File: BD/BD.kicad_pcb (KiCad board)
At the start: 2 copper layers, 95 x 90 mm, 57 parts, among them P1 bateria 7.4 V, P2 HC-06 (BT), P3 SILNIK1, P4 Modol startujacy, P5 PROGRAMAT, P7 SILNIK2, SW1 SPST, SW2 SW_PUSH, U1 LM1117, U10 TB6612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

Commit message: mozna drukowac?
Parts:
- moved R10 1.42 mm to (107.1, 66.6)
- moved R9 1.42 mm to (104.1, 66.6)
- moved U8 1.42 mm to (105.8, 63.7)
- turned C15 to 270 degrees
- turned C16 to 90 degrees
- turned C19 to 90 degrees
- turned C20 to 90 degrees
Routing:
- net SHARP4: track 43.7 -> 2.30 mm
- net GND: track 145.5 -> 182.6 mm, vias 2 -> 7
- net KTIR1: track 74.6 -> 95.8 mm
- net +5V: track 188.7 -> 174.5 mm
- net (no net): track 13.9 -> 0.00 mm, vias 5 -> 0
- net +3V3: track 458.2 -> 465.5 mm
- net BT2: track 33.5 -> 38.9 mm
- net PROG1: track 49.7 -> 55.0 mm
- net Net-(P3-Pad2): track 12.6 -> 7.67 mm, vias 1 -> 0
- net Net-(P3-Pad1): track 22.3 -> 17.9 mm, vias 1 -> 0
- net Net-(P7-Pad2): track 11.2 -> 6.88 mm, vias 1 -> 0
- net RESET: track 22.5 -> 26.3 mm
- net PROG2: track 39.5 -> 43.0 mm
- net VCC: track 132.8 -> 135.2 mm
- net KTIR2: track 72.5 -> 70.5 mm
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
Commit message: 2 wersja plytek
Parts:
- C1, C13, C2, C3, C4: footprint Capacitors_SMD:C_0402 -> Capacitors_SMD:C_0805_HandSoldering
- C10, C11, C12: footprint Capacitors_SMD:C_0603 -> Capacitors_SMD:C_0603_HandSoldering
- C14, C16, C18, C19, C22, C9: footprint Capacitors_SMD:C_0805 -> Capacitors_SMD:C_0805_HandSoldering
- C15, C17, C20, C21, C5, C6, C7, C8: footprint Capacitors_Tantalum_SMD:TantalC_SizeR_EIA-2012 -> Capacitors_Tantalum_SMD:Tantalum_Case-A_EIA-3216-18_Hand
- R1, R11, R12, R2, R3, R4, R5, R6: footprint Resistors_SMD:R_0805 -> Resistors_SMD:R_0805_HandSoldering
- R10, R7, R8, R9: footprint Resistors_SMD:R_0603 -> Resistors_SMD:R_0603_HandSoldering
- SP1: footprint Buzzer_moj -> Buzzers_Beepers:Buzzer_12x9.5RM7.6
- moved C17 3.79 mm to (171.1, 130.6), turned to 270 degrees
- moved C15 3.54 mm to (124.4, 130.2), turned to 90 degrees
- moved C16 2.87 mm to (126.8, 132.2)
- moved C14 2.21 mm to (144.6, 121.6)
- moved C13 2.01 mm to (144.6, 119.3)
- moved C19 1.35 mm to (127.2, 137.7)
- moved C18 1.26 mm to (168.1, 134.3)
- moved C22 0.75 mm to (167.8, 139.8)
- moved R2 0.73 mm to (115.2, 100.7)
- moved R9 0.72 mm to (103.4, 66.6)
- moved R10 0.65 mm to (107.8, 66.6)
- moved C10 0.59 mm to (155.2, 107.1)
- moved C4 0.59 mm to (168.7, 90.1)
- moved C21 0.44 mm to (171.0, 138.9), turned to 90 degrees
- moved C2 0.39 mm to (115.2, 105.9)
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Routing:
- net SHARP4: track 2.30 -> 55.7 mm
- net +3V3: track 465.5 -> 501.6 mm, vias 5 -> 6
- net +5V: track 174.5 -> 192.3 mm
- net GND: track 182.6 -> 196.2 mm
- net SHARP1: track 40.6 -> 51.2 mm
- net VCC: track 135.2 -> 141.5 mm, vias 2 -> 3
- net Net-(D1-Pad2): track 5.71 -> 10.8 mm
- net RESET: track 26.3 -> 30.9 mm, vias 0 -> 1
- net KTIR1: track 95.8 -> 97.8 mm
- net PROG1: track 55.0 -> 54.1 mm
- net Net-(R2-Pad1): track 7.24 -> 6.48 mm
- net SHARP3: track 49.8 -> 50.5 mm
- net Net-(R12-Pad1): track 20.3 -> 20.9 mm

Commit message: tak
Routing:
- net +3V3: track 501.6 -> 488.2 mm, vias 6 -> 4
- net GND: track 196.2 -> 193.2 mm, vias 7 -> 6
- net VCC: track 141.5 -> 139.1 mm, vias 3 -> 2
- net RESET: track 30.9 -> 32.1 mm
- net KTIR1: track 97.8 -> 98.4 mm
- net +5V: track 192.3 -> 192.7 mm, vias 7 -> 4

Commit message: taak
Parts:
- moved P1 1.25 mm to (137.4, 91.8)
- moved SW1 0.50 mm to (137.4, 99.4), turned to 180 degrees
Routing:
- net +5V: track 192.7 -> 185.5 mm
- net VCC: track 139.1 -> 144.8 mm
- net GND: track 193.2 -> 190.3 mm
- net Net-(P1-Pad2): track 6.35 -> 5.11 mm
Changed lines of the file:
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@@
     (thickness 1.6)
     (drawings 14)
-    (tracks 775)
+    (tracks 776)
     (zones 0)
     (modules 57)
@@
   )
   (module Socket_Strips:Socket_Strip_Straight_1x02 (layer F.Cu)
-    (at 137.85 90.61 270)
+    (at 137.41 91.78 270)
     (descr "Through hole socket strip")
     (tags "socket strip")
@@
   )
   (module Buttons_Switches_ThroughHole:SW_DIP_x1_Slide (layer F.Cu)
-    (at 137.86 99.48 270)
+    (at 137.36 99.41 180)
     (descr "CTS Electrocomponents, Series 206/208")
-    (fp_text reference SW1 (at 0 -10 270) (layer F.SilkS)
-      (effects (font (size 1 1) (thickness 0.15)))
-    )
-    (fp_text value SPST (at 0.5 2.4 270) (layer F.Fab)
+    (fp_text reference SW1 (at 0 -10 180) (layer F.SilkS)
+      (effects (font (size 1 1) (thickness 0.15)))
+    )
+    (fp_text value SPST (at 0.5 2.4 180) (layer F.Fab)
       (effects (font (size 1 1) (thickness 0.15)))
     )
@@
     (fp_line (start 0.64 -1.78) (end 0.64 -5.84) (layer F.SilkS) (width 0.15))
     (fp_line (start 0.64 -5.84) (end -0.64 -5.84) (layer F.SilkS) (width 0.15))
-    (pad 1 thru_hole rect (at 0 0 270) (size 1.524 1.824) (drill 0.762) (layers *.Cu *.Mask)
+    (pad 1 thru_hole rect (at 0 0 180) (size 1.524 1.824) (drill 0.762) (layers *.Cu *.Mask)
       (net 13 "Net-(P1-Pad2)"))
-    (pad 2 thru_hole oval (at 0 -7.62 270) (size 1.524 1.824) (drill 0.762) (layers *.Cu *.Mask)
+    (pad 2 thru_hole oval (at 0 -7.62 180) (size 1.524 1.824) (drill 0.762) (layers *.Cu *.Mask)
       (net 6 VCC))
     (model Buttons_Switches_ThroughHole.3dshapes/SW_DIP_x1_Slide.wrl
@@
   (gr_line (start 165 150) (end 115 150) (layer Edge.Cuts) (width 0.15))
   (gr_line (start 100 60) (end 195 60) (layer Edge.Cuts) (width 0.15))
+  (segment (start 137.41 91.78) (end 142.126398 91.78) (width 0.889) (layer F.Cu) (net 1))
+  (segment (start 142.126398 91.78) (end 142.334568 91.57183) (width 0.889) (layer F.Cu) (net 1))
   (segment (start 121.4835 85.1435) (end 121.4835 87.4435) (width 0.4064) (layer F.Cu) (net 1))
   (segment (start 121.4835 87.4435) (end 124.09 90.05) (width 0.4064) (layer F.Cu) (net 1))
@@
   (segment (start 143.475 119.29) (end 143.35 119.29) (width 0.4064) (layer F.Cu) (net 1))
   (segment (start 181.35 101.69) (end 181.35 99.36) (width 0.4064) (layer F.Cu) (net 1))
-  (segment (start 143.184568 87.74183) (end 140.71817 87.74183) (width 0.889) (layer F.Cu) (net 1))
-  (segment (start 140.71817 87.74183) (end 137.85 90.61) (width 0.889) (layer F.Cu) (net 1))
   (segment (start 142.334568 91.57183) (end 142.334568 88.59183) (width 0.889) (layer F.Cu) (net 1))
   (segment (start 142.334568 88.59183) (end 143.184568 87.74183) (width 0.889) (layer F.Cu) (net 1))
@@
   (segment (start 148.14 114.926) (end 148.14 115.78) (width 0.254) (layer F.Cu) (net 1))
   (segment (start 143.158548 87.76785) (end 143.184568 87.74183) (width 0.4064) (layer F.Cu) (net 1))
-  (segment (start 138.81183 91.57183) (end 137.85 90.61) (width 0.4064) (layer F.Cu) (net 1))
   (segment (start 152.830009 109.254773) (end 152.501601 109.257001) (width 0.254) (layer F.Cu) (net 1))
   (segment (start 154.96 108.34) (end 153.949617 108.34) (width 0.4064) (layer F.Cu) (net 1))
@@
   (segment (start 167.5 84.9435) (end 167.5 89.95) (width 0.4064) (layer F.Cu) (net 5))
   (segment (start 167.5 89.95) (end 167.55 90) (width 0.4064) (layer F.Cu) (net 5))
+  (segment (start 139.79 107.1) (end 140.58 107.1) (width 0.889) (layer B.Cu) (net 6))
+  (segment (start 141.3 105.59) (end 141.64 105.59) (width 0.889) (layer B.Cu) (net 6))
+  (segment (start 141.64 105.59) (end 148.86 98.37) (width 0.889) (layer B.Cu) (net 6))
+  (segment (start 141.3 105.59) (end 141.3 108.33) (width 0.889) (layer B.Cu) (net 6))
+  (segment (start 141.3 108.33) (end 141.3 118.95) (width 0.889) (layer B.Cu) (net 6))
+  (segment (start 139.79 107.1) (end 140.07 107.1) (width 0.889) (layer B.Cu) (net 6))
+  (segment (start 140.07 107.1) (end 141.3 108.33) (width 0.889) (layer B.Cu) (net 6))
+  (segment (start 141.3 105.59) (end 139.79 107.1) (width 0.889) (layer B.Cu) (net 6))
+  (segment (start 139.79 107.1) (end 137.86 107.1) (width 0.889) (layer B.Cu) (net 6))
   (segment (start 147.02 135.512102) (end 147.02 130.73) (width 0.889) (layer F.Cu) (net 6))
   (segment (start 147.02 130.73) (end 149.410001 128.339999) (width 0.889) (layer F.Cu) (net 6))
@@
   (segment (start 148.86 98.37) (end 148.86 97.583282) (width 0.889) (layer F.Cu) (net 6))
   (segment (start 148.86 97.583282) (end 146.308548 95.03183) (width 0.889) (layer F.Cu) (net 6))
-  (segment (start 145.48 99.48) (end 147.75 99.48) (width 0.889) (layer B.Cu) (net 6))
-  (segment (start 147.75 99.48) (end 148.86 98.37) (width 0.889) (layer B.Cu) (net 6))
   (via (at 148.86 98.37) (size 1.3) (drill 0.5) (layers F.Cu B.Cu) (net 6))
   (segment (start 146.308548 95.03183) (end 147.297239 95.03183) (width 0.889) (layer F.Cu) (net 6))
@@
   (segment (start 141.3 118.95) (end 146.91 124.56) (width 0.889) (layer B.Cu) (net 6))
   (segment (start 160.998169 132.900782) (end 160.998169 136.564695) (width 0.3048) (layer F.Cu) (net 6))
-  (segment (start 141.3 105.59) (end 141.3 118.95) (width 0.889) (layer B.Cu) (net 6))
-  (segment (start 145.48 101.41) (end 141.3 105.59) (width 0.889) (layer B.Cu) (net 6))
-  (segment (start 145.48 99.48) (end 145.48 101.41) (width 0.889) (layer B.Cu) (net 6))
+  (segment (start 150.3 88.91) (end 131 88.91) (width 0.889) (layer B.Cu) (net 7))
+  (segment (start 131 88.91) (end 128.99 90.92) (width 0.889) (layer B.Cu) (net 7))
   (segment (start 160.56 99.19) (end 158.95 97.58) (width 0.889) (layer B.Cu) (net 7))
   (segment (start 158.95 97.58) (end 157.05 97.58) (width 0.889) (layer B.Cu) (net 7))
@@
   (segment (start 154.300001 94.830001) (end 157.05 97.58) (width 0.889) (layer B.Cu) (net 7))
   (segment (start 154.300001 94.780001) (end 154.300001 94.830001) (width 0.889) (layer B.Cu) (net 7))
-  (segment (start 137.46 102.27) (end 138.81 102.27) (width 0.889) (layer B.Cu) (net 7))
-  (segment (start 138.81 102.27) (end 150.3 90.78) (width 0.889) (layer B.Cu) (net 7))
-  (segment (start 129.11 93.92) (end 137.46 102.27) (width 0.889) (layer B.Cu) (net 7))
   (segment (start 145.484568 87.74183) (end 145.484568 89.73083) (width 0.889) (layer F.Cu) (net 7))
   (segment (start 145.484568 89.73083) (end 146.599597 90.845859) (width 0.889) (layer F.Cu) (net 7))
@@
   (segment (start 169.51 112.92) (end 169.51 116.28) (width 0.4064) (layer B.Cu) (net 12))
   (segment (start 169.51 116.28) (end 174.9 121.67) (width 0.4064) (layer B.Cu) (net 12))
-  (segment (start 137.85 93.15) (end 137.85 99.47) (width 0.889) (layer B.Cu) (net 13))
-  (segment (start 137.85 99.47) (end 137.86 99.48) (width 0.889) (layer B.Cu) (net 13))
-  (segment (start 137.86 93.16) (end 137.85 93.15) (width 0.889) (layer F.Cu) (net 13))
+  (segment (start 137.41 94.32) (end 137.41 99.36) (width 0.889) (layer B.Cu) (net 13))
+  (segment (start 137.41 99.36) (end 137.36 99.41) (width 0.889) (layer B.Cu) (net 13))
   (segment (start 125.570608 118.82062) (end 124.05938 118.82062) (width 0.4064) (layer B.Cu) (net 14))
   (segment (start 124.05938 118.82062) (end 118.71 124.17) (width 0.4064) (layer B.Cu) (net 14))

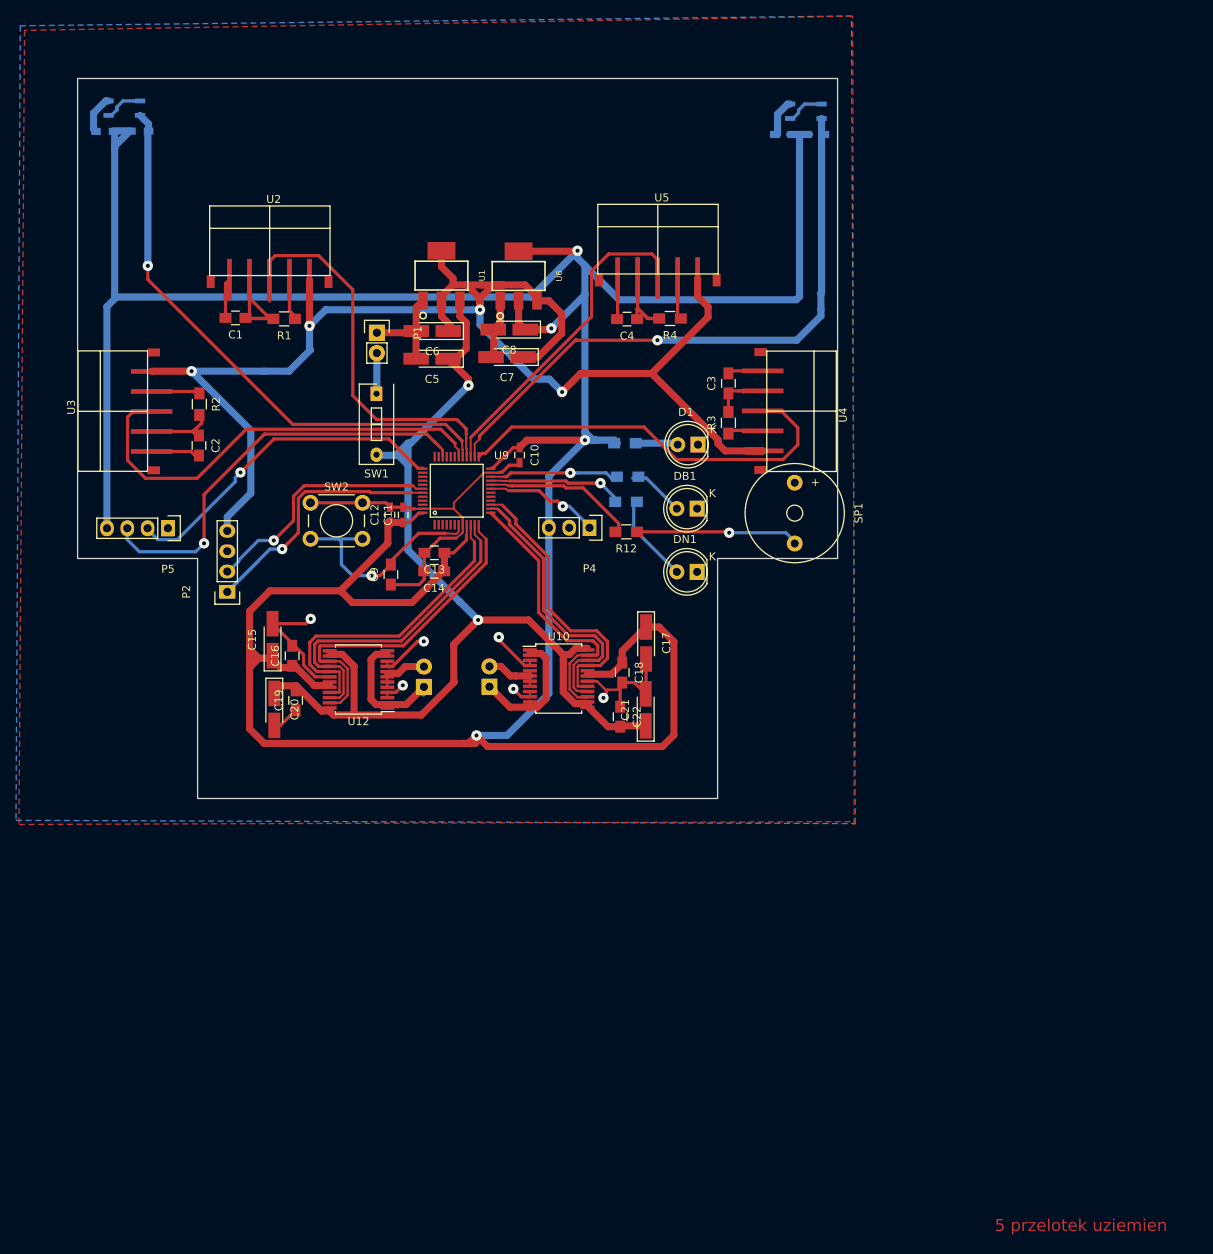
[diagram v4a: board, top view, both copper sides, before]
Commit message: Stabilizatory na dnie
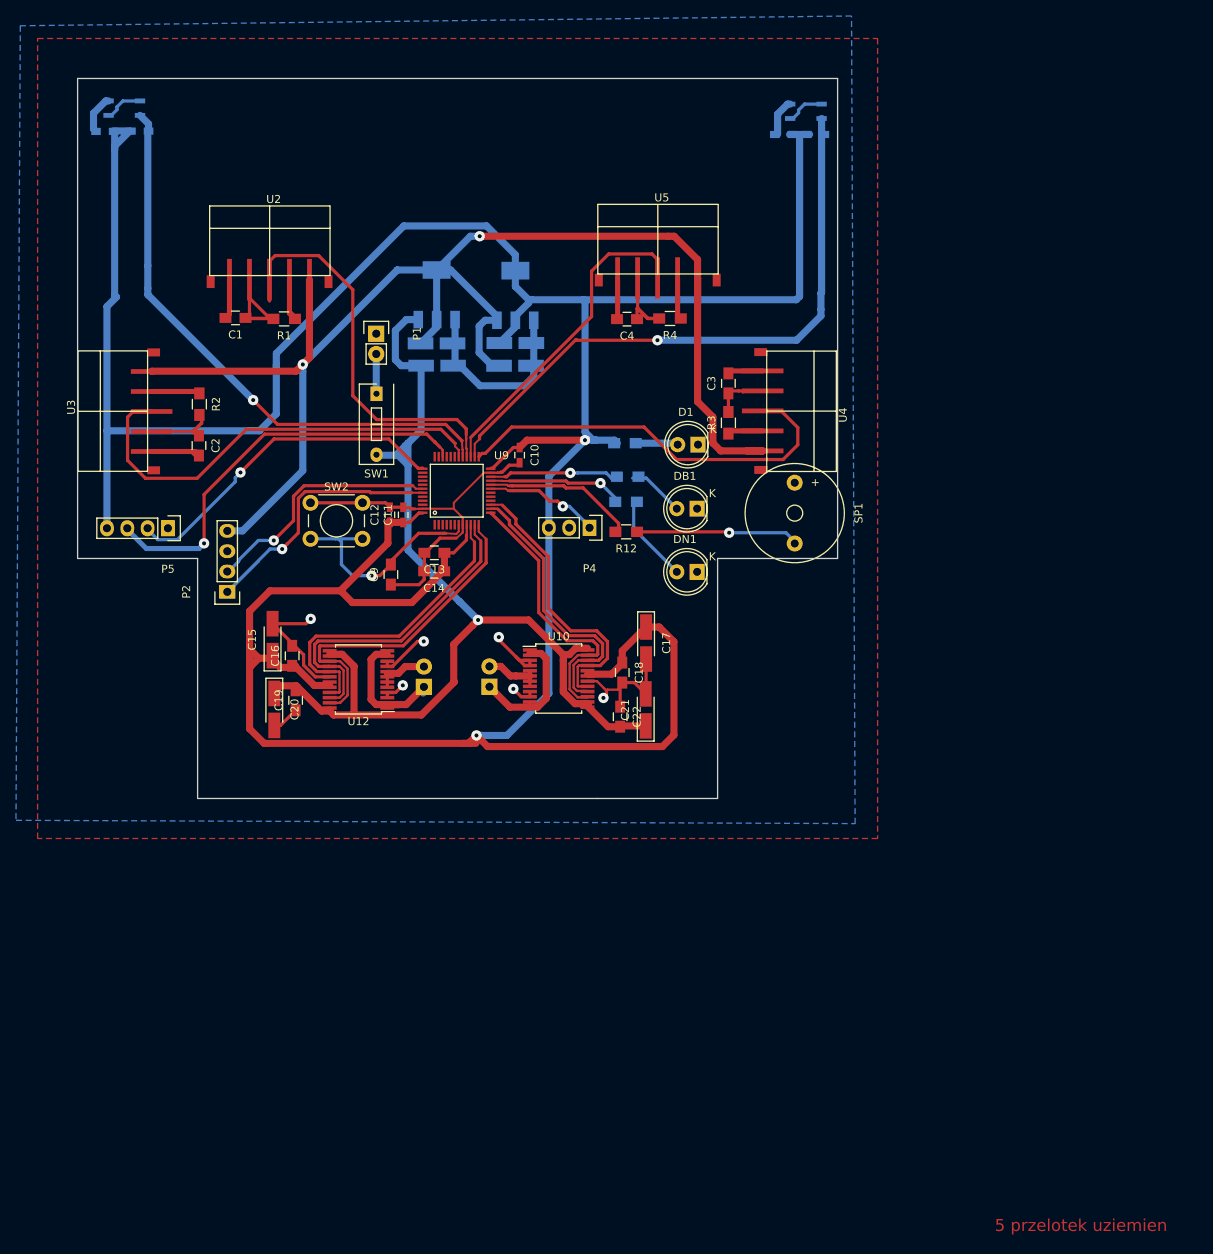
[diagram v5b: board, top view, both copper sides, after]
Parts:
- C5, C6, C7, C8, U1, U6: moved to B.Cu
- moved U1 2.47 mm to (144.9, 87.0)
- moved U6 2.46 mm to (154.7, 87.1)
- moved C8 1.84 mm to (154.7, 93.1), turned to 0 degrees
- moved C6 1.63 mm to (144.9, 93.1), turned to 0 degrees
- moved C7 1.48 mm to (154.7, 95.9), turned to 0 degrees
- moved C5 1.07 mm to (144.9, 95.9), turned to 0 degrees
- moved P1 0.14 mm to (137.3, 91.9)
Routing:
- net +3V3: track 488.2 -> 445.4 mm, vias 4 -> 2
- net +5V: track 185.5 -> 177.4 mm, vias 4 -> 2
- net Net-(C2-Pad2): track 6.12 -> 12.2 mm
- net Net-(R2-Pad1): track 6.48 -> 12.5 mm
- net Net-(R4-Pad1): track 5.06 -> 10.3 mm
- net Net-(R1-Pad1): track 5.19 -> 10.4 mm
- net Net-(C4-Pad2): track 5.08 -> 10.2 mm
- net Net-(R3-Pad1): track 4.31 -> 8.74 mm
- net VCC: track 144.8 -> 142.8 mm, vias 2 -> 1
- net Net-(P7-Pad2): track 6.88 -> 8.83 mm
- net Net-(P3-Pad2): track 7.67 -> 8.97 mm
- net PROG1: track 54.1 -> 52.9 mm
- net KTIR2: track 70.7 -> 71.8 mm
- net GND: track 190.3 -> 191.4 mm
- net Net-(P7-Pad1): track 18.5 -> 19.4 mm

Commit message: Poprawilem jeszcze jedno polaczenie gnd,jest dobrze teraz, sprawdzaj
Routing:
- net GND: track 191.4 -> 228.7 mm, vias 6 -> 7
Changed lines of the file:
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@@
     (thickness 1.6)
     (drawings 14)
-    (tracks 763)
+    (tracks 774)
     (zones 0)
     (modules 57)
@@
   )
   (setup
-    (last_trace_width 0.889)
+    (last_trace_width 0.254)
     (user_trace_width 0.254)
     (user_trace_width 0.3048)
@@
   (gr_line (start 165 150) (end 115 150) (layer Edge.Cuts) (width 0.15))
   (gr_line (start 100 60) (end 195 60) (layer Edge.Cuts) (width 0.15))
+  (segment (start 115.32 81.3) (end 119.94 81.3) (width 0.254) (layer F.Cu) (net 1))
+  (segment (start 119.94 81.3) (end 121.4835 82.8435) (width 0.254) (layer F.Cu) (net 1))
+  (segment (start 121.4835 82.8435) (end 121.4835 85.1435) (width 0.254) (layer F.Cu) (net 1))
+  (segment (start 114.403501 82.216499) (end 115.32 81.3) (width 0.254) (layer F.Cu) (net 1))
+  (segment (start 112.09 84.52) (end 114.393501 82.216499) (width 0.254) (layer F.Cu) (net 1))
+  (segment (start 114.393501 82.216499) (end 114.403501 82.216499) (width 0.254) (layer F.Cu) (net 1))
+  (segment (start 107.8 62.81) (end 108.15 62.81) (width 0.254) (layer B.Cu) (net 1))
+  (segment (start 112.09 67.1) (end 112.09 84.52) (width 0.254) (layer B.Cu) (net 1))
+  (segment (start 108.15 62.81) (end 112.09 66.75) (width 0.254) (layer B.Cu) (net 1))
+  (via (at 112.09 84.52) (size 1.3) (drill 0.5) (layers F.Cu B.Cu) (net 1))
+  (segment (start 112.09 66.75) (end 112.09 67.1) (width 0.254) (layer B.Cu) (net 1))
   (segment (start 155.89 133.385) (end 154.85 132.345) (width 0.4064) (layer F.Cu) (net 1))
   (segment (start 154.85 132.345) (end 152.65 130.145) (width 0.4064) (layer F.Cu) (net 1))
